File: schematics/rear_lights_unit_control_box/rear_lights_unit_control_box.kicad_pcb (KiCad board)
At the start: 2 copper layers, 50.8 x 50.8 mm, 7 parts, among them J1 Conn_01x04_Socket, SW1 SW_SPDT, SW2 SW_SPDT

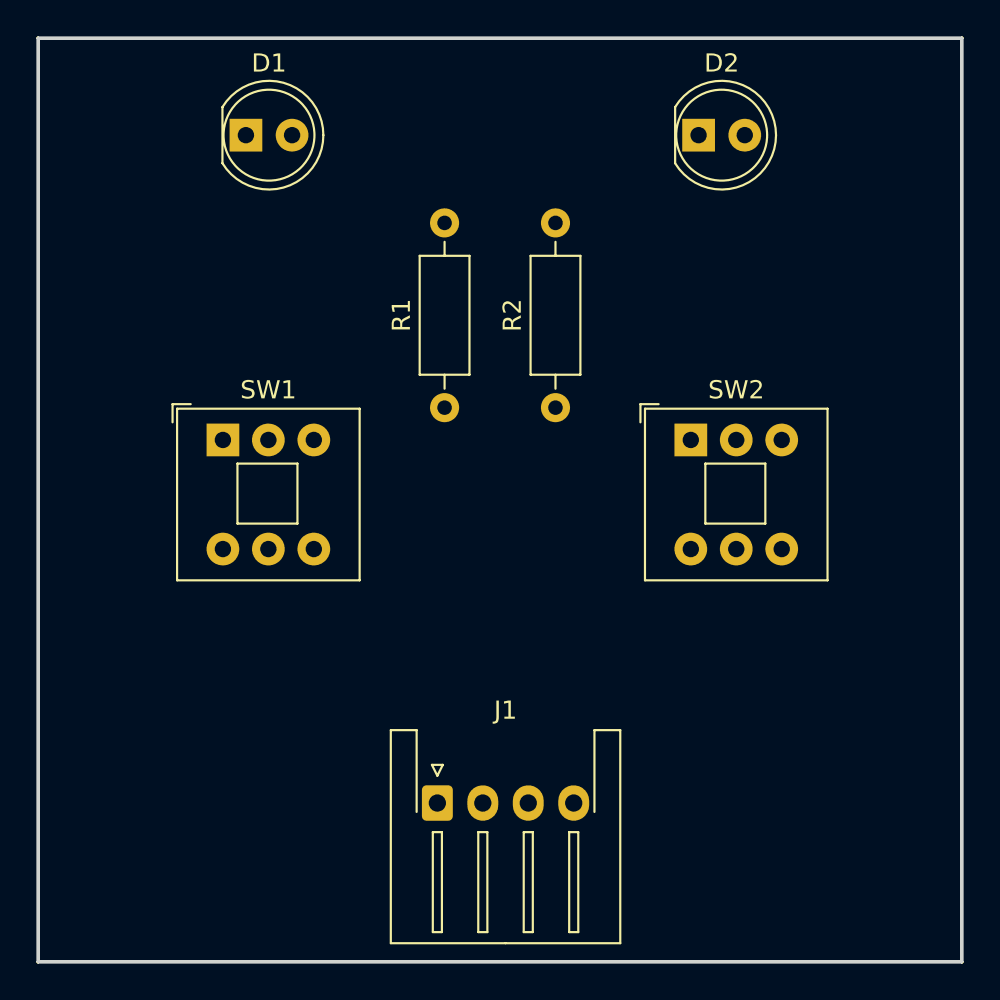
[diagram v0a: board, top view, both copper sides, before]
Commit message: rear light unit control box: finished first draft of PCB
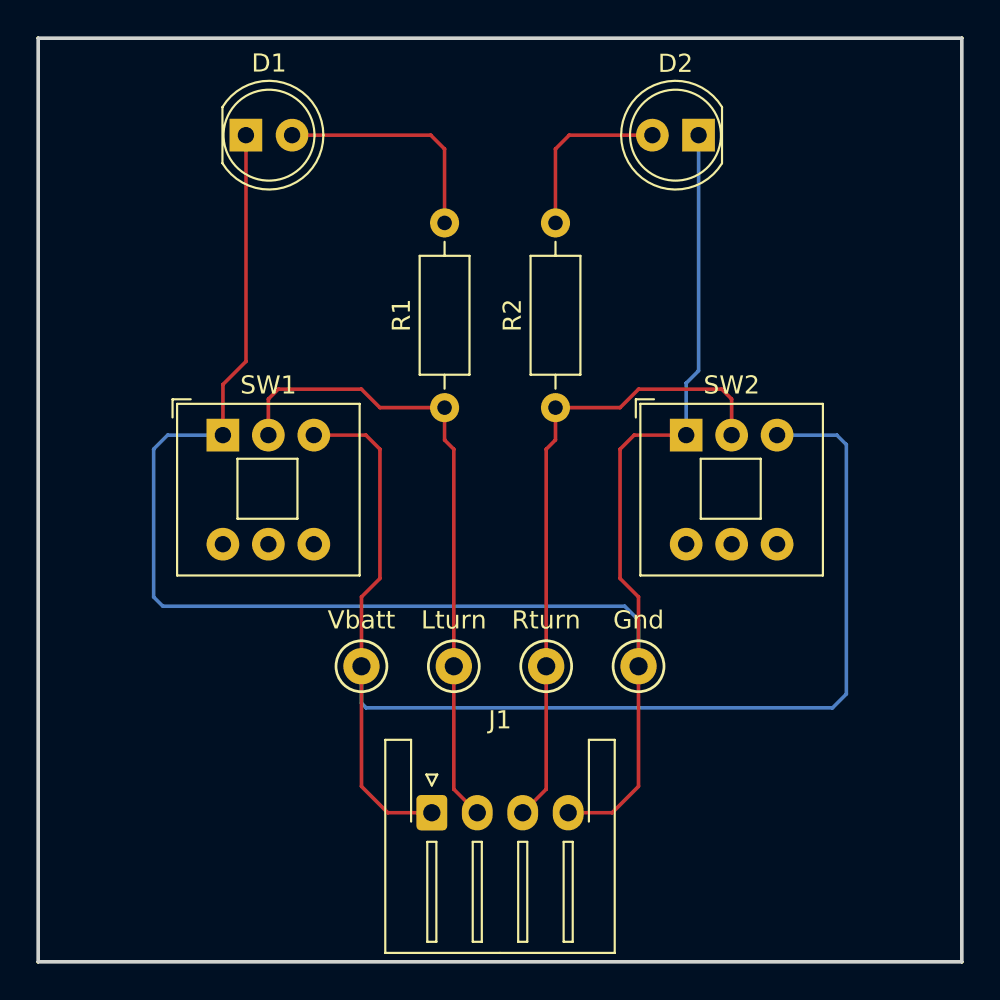
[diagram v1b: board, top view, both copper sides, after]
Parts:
- added G***: LOGO, FarrhadTech:resisty_0.5x0.65inch, B.Cu at (145.0, 94.0)
- added TP1: Vbatt, TestPoint:TestPoint_Keystone_5000-5004_Miniature, F.Cu at (119.4, 85.3)
- added TP2: Lturn, TestPoint:TestPoint_Keystone_5000-5004_Miniature, F.Cu at (124.5, 85.3)
- added TP3: Rturn, TestPoint:TestPoint_Keystone_5000-5004_Miniature, F.Cu at (129.5, 85.3)
- added TP4: Gnd, TestPoint:TestPoint_Keystone_5000-5004_Miniature, F.Cu at (134.6, 85.3)
- moved J1 0.61 mm to (123.2, 93.4)
- moved SW2 0.37 mm to (137.2, 72.6)
- moved SW1 0.27 mm to (111.8, 72.6)
- turned D2 to 180 degrees
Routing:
- net GND: track 0.00 -> 103.2 mm
- net V_OUT: track 0.00 -> 74.3 mm
- net RIGHT_TURN_EN: track 0.00 -> 35.4 mm
- net LEFT_TURN_EN: track 0.00 -> 35.4 mm
- net Net-(D1-A): track 0.00 -> 12.8 mm
- net Net-(D2-A): track 0.00 -> 9.71 mm
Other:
- board text added: "FarrhadTech Rear Light Unit Control Box v0"

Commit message: rear light unit control box PCB finalized!
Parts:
- added REF**: 3mm, MountingHole:MountingHole_3mm, F.Cu at (148.1, 55.1)
- added REF**: 3mm, MountingHole:MountingHole_3mm, F.Cu at (148.1, 94.5)
- added REF**: 3mm, MountingHole:MountingHole_3mm, F.Cu at (105.9, 94.5)
- added REF**: 3mm, MountingHole:MountingHole_3mm, F.Cu at (105.9, 55.1)
- TP1: value Vbatt -> VBATT
- TP2: value Lturn -> LEFT
- TP3: value Rturn -> RIGHT
- TP4: value Gnd -> GND
- moved R2 12.1 mm to (139.5, 63.5), turned to 180 degrees
- moved R1 7.68 mm to (125.2, 63.5), turned to 180 degrees
- moved G*** 6.18 mm to (139.8, 90.7)
- moved SW1 3.13 mm to (113.3, 69.9)
- moved SW2 3.13 mm to (135.7, 69.9)
- moved D2 3.05 mm to (141.0, 56.1)
- moved J1 2.75 mm to (123.2, 90.7)
- moved TP1 2.75 mm to (119.4, 82.6)
- moved TP2 2.75 mm to (124.5, 82.6)
- moved TP3 2.75 mm to (129.5, 82.6)
- moved TP4 2.75 mm to (134.6, 82.6)
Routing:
- net GND: track 103.2 -> 94.3 mm
- net RIGHT_TURN_EN: track 35.4 -> 42.1 mm
- net V_OUT: track 74.3 -> 67.6 mm
- net Net-(D2-A): track 9.71 -> 16.1 mm
- net LEFT_TURN_EN: track 35.4 -> 41.6 mm
- net Net-(D1-A): track 12.8 -> 7.64 mm
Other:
- board size 50.8 x 50.8 mm -> 50.8 x 48 mm
- board text added: "LED"

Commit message: updated both sets of light unit board files to include the newly-added 3D models
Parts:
- TP1, TP2, TP3, TP4: footprint TestPoint:TestPoint_Keystone_5000-5004_Miniature -> FahrradTech:TestPoint_Keystone_5000-5004_Miniature
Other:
- board text added: "FahrradTech Rear Light Unit Control Box v0"
- board text removed: "FarrhadTech Rear Light Unit Control Box v0"
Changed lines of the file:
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@@
 		)
 	)
-	(footprint "TestPoint:TestPoint_Keystone_5000-5004_Miniature"
+	(footprint "FahrradTech:TestPoint_Keystone_5000-5004_Miniature"
 		(layer "F.Cu")
 		(at 124.46 82.594)
@@
 			)
 		)
-		(property "Footprint" "TestPoint:TestPoint_Keystone_5000-5004_Miniature"
+		(property "Footprint" "FahrradTech:TestPoint_Keystone_5000-5004_Miniature"
 			(at 0 0 0)
 			(unlocked yes)
@@
 			(pintype "passive")
 		)
-		(model "${KICAD8_3DMODEL_DIR}/TestPoint.3dshapes/TestPoint_Keystone_5000-5004_Miniature.wrl"
+		(model "${KICAD8_3DMODEL_DIR}/TestPoint.3dshapes/TestPoint_Keystone_5005-5009_Compact.step"
 			(offset
 				(xyz 0 0 0)
@@
 		)
 	)
-	(footprint "TestPoint:TestPoint_Keystone_5000-5004_Miniature"
+	(footprint "FahrradTech:TestPoint_Keystone_5000-5004_Miniature"
 		(layer "F.Cu")
 		(at 134.62 82.594)
@@
 			)
 		)
-		(property "Footprint" "TestPoint:TestPoint_Keystone_5000-5004_Miniature"
+		(property "Footprint" "FahrradTech:TestPoint_Keystone_5000-5004_Miniature"
 			(at 0 0 0)
 			(unlocked yes)
@@
 			(pintype "passive")
 		)
-		(model "${KICAD8_3DMODEL_DIR}/TestPoint.3dshapes/TestPoint_Keystone_5000-5004_Miniature.wrl"
+		(model "${KICAD8_3DMODEL_DIR}/TestPoint.3dshapes/TestPoint_Keystone_5005-5009_Compact.step"
 			(offset
 				(xyz 0 0 0)
@@
 		)
 	)
-	(footprint "TestPoint:TestPoint_Keystone_5000-5004_Miniature"
+	(footprint "FahrradTech:TestPoint_Keystone_5000-5004_Miniature"
 		(layer "F.Cu")
 		(at 119.38 82.594)
@@
 			)
 		)
-		(property "Footprint" "TestPoint:TestPoint_Keystone_5000-5004_Miniature"
+		(property "Footprint" "FahrradTech:TestPoint_Keystone_5000-5004_Miniature"
 			(at 0 0 0)
 			(unlocked yes)
@@
 			(pintype "passive")
 		)
-		(model "${KICAD8_3DMODEL_DIR}/TestPoint.3dshapes/TestPoint_Keystone_5000-5004_Miniature.wrl"
+		(model "${KICAD8_3DMODEL_DIR}/TestPoint.3dshapes/TestPoint_Keystone_5005-5009_Compact.step"
 			(offset
 				(xyz 0 0 0)
@@
 		)
 	)
-	(footprint "TestPoint:TestPoint_Keystone_5000-5004_Miniature"
+	(footprint "FahrradTech:TestPoint_Keystone_5000-5004_Miniature"
 		(layer "F.Cu")
 		(at 129.54 82.594)
@@
 			)
 		)
-		(property "Footprint" "TestPoint:TestPoint_Keystone_5000-5004_Miniature"
+		(property "Footprint" "FahrradTech:TestPoint_Keystone_5000-5004_Miniature"
 			(at 0 0 0)
 			(unlocked yes)
@@
 			(pintype "passive")
 		)
-		(model "${KICAD8_3DMODEL_DIR}/TestPoint.3dshapes/TestPoint_Keystone_5000-5004_Miniature.wrl"
+		(model "${KICAD8_3DMODEL_DIR}/TestPoint.3dshapes/TestPoint_Keystone_5005-5009_Compact.step"
 			(offset
 				(xyz 0 0 0)
@@
 		(layer "F.Fab")
 	)
-	(gr_text "FarrhadTech Rear Light\nUnit Control Box v0"
+	(gr_text "FahrradTech Rear Light\nUnit Control Box v0"
 		(at 135 95.5 0)
 		(layer "B.SilkS")
